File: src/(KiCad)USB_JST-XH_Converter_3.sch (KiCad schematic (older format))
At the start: 10 parts

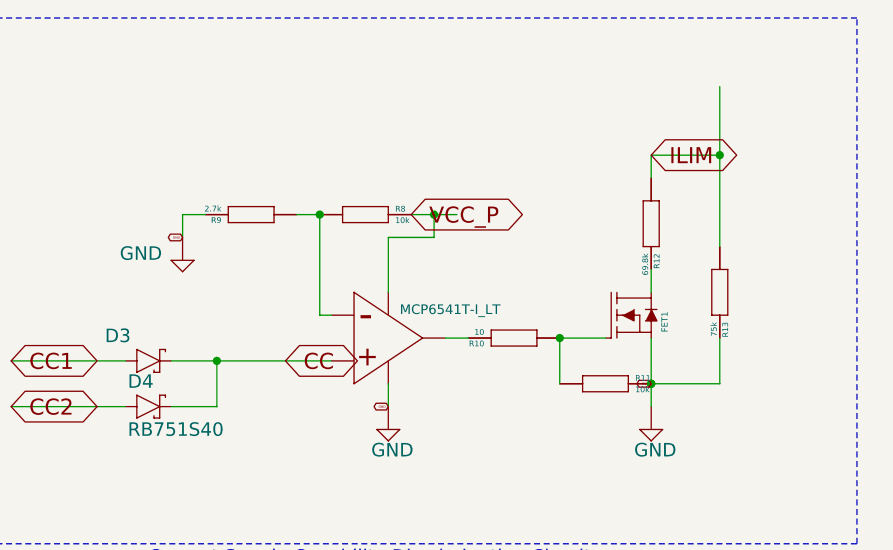
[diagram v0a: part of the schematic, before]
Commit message: 3Aモード用LEDの追加
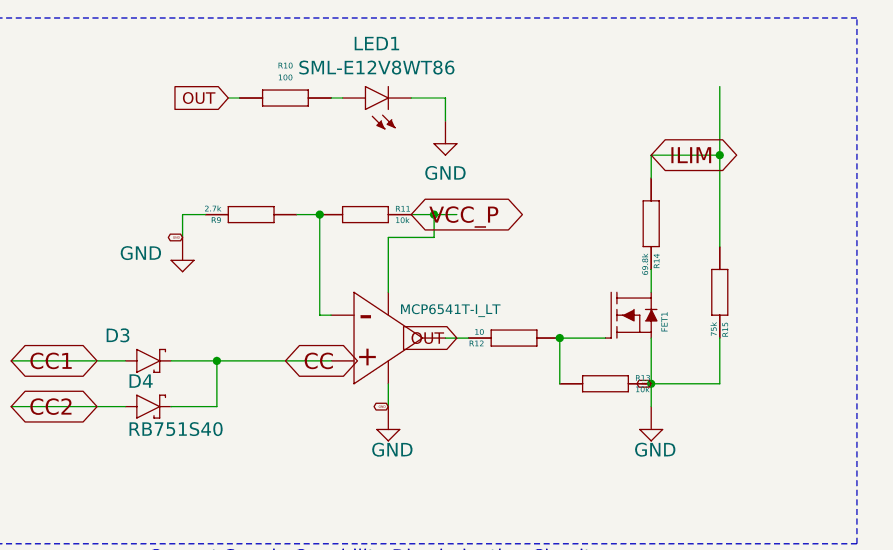
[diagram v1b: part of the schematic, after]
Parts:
- added LED1: SML-E12V8WT86, USB_JST-XH_Converter:SML-E12V8WT86, symbol USB_JST-XH_Converter-eagle-import:SML-E12V8WT86
- added R10: 100, USB_JST-XH_Converter:RG2012, symbol USB_JST-XH_Converter-eagle-import:RG2012
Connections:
- net labels added: OUT
- wire segments 29 -> 33
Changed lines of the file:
@@
 $Descr A4 11693 8268
 encoding utf-8
-Sheet 1 4
+Sheet 4 4
 Title ""
 Date ""
@@
 	7100 3700 6800 3700
 Connection ~ 6800 3700
-Connection ~ 6800 3700
 Text GLabel 6800 3700 0    10   BiDi ~ 0
 GND
@@
 AR Path="/5B1AAE1E" Ref="#FRAME3"  Part="1"
 AR Path="/639B4E7B/5B1AAE1E" Ref="#FRAME3"  Part="1"
+AR Path="/639ECBA2/5B1AAE1E" Ref="#FRAME3"  Part="1"
 F 0 "#FRAME3" H 2300 6000 50  0001 C CNN
 F 1 "A5L-LOC" H 2300 6000 50  0001 C CNN
@@
 AR Path="/3097C624" Ref="R8"  Part="1"
 AR Path="/639B4E7B/3097C624" Ref="R8"  Part="1"
-F 0 "R8" H 5680 2970 25  0000 L BNN
+AR Path="/639ECBA2/3097C624" Ref="R11"  Part="1"
+F 0 "R11" H 5680 2970 25  0000 L BNN
 F 1 "10k" H 5680 2920 25  0000 L BNN
 F 2 "USB_JST-XH_Converter:RG2012" H 5550 2960 50  0001 C CNN
@@
 AR Path="/1BCD2ED9" Ref="R9"  Part="1"
 AR Path="/639B4E7B/1BCD2ED9" Ref="R9"  Part="1"
+AR Path="/639ECBA2/1BCD2ED9" Ref="R9"  Part="1"
 F 0 "R9" H 5180 2970 25  0000 L BNN
 F 1 "2.7k" H 5180 2920 25  0000 L BNN
@@
 AR Path="/28999800" Ref="#SUPPLY10"  Part="1"
 AR Path="/639B4E7B/28999800" Ref="#SUPPLY010"  Part="1"
-F 0 "#SUPPLY010" H 4750 3160 50  0001 C CNN
+AR Path="/639ECBA2/28999800" Ref="#SUPPLY0111"  Part="1"
+F 0 "#SUPPLY0111" H 4750 3160 50  0001 C CNN
 F 1 "GND" H 4475 3155 59  0000 L BNN
 F 2 "" H 4750 3160 50  0001 C CNN
@@
 AR Path="/E0B04C0E" Ref="#SUPPLY11"  Part="1"
 AR Path="/639B4E7B/E0B04C0E" Ref="#SUPPLY011"  Part="1"
-F 0 "#SUPPLY011" H 5650 3900 50  0001 C CNN
+AR Path="/639ECBA2/E0B04C0E" Ref="#SUPPLY0112"  Part="1"
+F 0 "#SUPPLY0112" H 5650 3900 50  0001 C CNN
 F 1 "GND" H 5575 3775 59  0000 L BNN
 F 2 "" H 5650 3900 50  0001 C CNN
@@
 AR Path="/B5DC468C" Ref="R10"  Part="1"
 AR Path="/639B4E7B/B5DC468C" Ref="R10"  Part="1"
-F 0 "R10" H 6330 3510 25  0000 L BNN
+AR Path="/639ECBA2/B5DC468C" Ref="R12"  Part="1"
+F 0 "R12" H 6330 3510 25  0000 L BNN
 F 1 "10" H 6330 3460 25  0000 L BNN
 F 2 "USB_JST-XH_Converter:RG2012" H 6200 3500 50  0001 C CNN
@@
 AR Path="/369C72E5" Ref="R11"  Part="1"
 AR Path="/639B4E7B/369C72E5" Ref="R11"  Part="1"
-F 0 "R11" H 6730 3710 25  0000 L BNN
+AR Path="/639ECBA2/369C72E5" Ref="R13"  Part="1"
+F 0 "R13" H 6730 3710 25  0000 L BNN
 F 1 "10k" H 6730 3660 25  0000 L BNN
 F 2 "USB_JST-XH_Converter:RG2012" H 6600 3700 50  0001 C CNN
@@
 AR Path="/87B19EEA" Ref="R12"  Part="1"
 AR Path="/639B4E7B/87B19EEA" Ref="R12"  Part="1"
-F 0 "R12" H 6930 3010 25  0000 L BNN
+AR Path="/639ECBA2/87B19EEA" Ref="R14"  Part="1"
+F 0 "R14" H 6930 3010 25  0000 L BNN
 F 1 "69.8k" H 6930 2960 25  0000 L BNN
 F 2 "USB_JST-XH_Converter:RG2012" H 6800 3000 50  0001 C CNN
@@
 AR Path="/EFAC6E10" Ref="R13"  Part="1"
 AR Path="/639B4E7B/EFAC6E10" Ref="R13"  Part="1"
-F 0 "R13" H 7230 3310 25  0000 L BNN
+AR Path="/639ECBA2/EFAC6E10" Ref="R15"  Part="1"
+F 0 "R15" H 7230 3310 25  0000 L BNN
 F 1 "75k" H 7230 3260 25  0000 L BNN
 F 2 "USB_JST-XH_Converter:RG2012" H 7100 3300 50  0001 C CNN
@@
 AR Path="/31C2C8A5" Ref="#SUPPLY12"  Part="1"
 AR Path="/639B4E7B/31C2C8A5" Ref="#SUPPLY012"  Part="1"
-F 0 "#SUPPLY012" H 6800 3900 50  0001 C CNN
+AR Path="/639ECBA2/31C2C8A5" Ref="#SUPPLY0113"  Part="1"
+F 0 "#SUPPLY0113" H 6800 3900 50  0001 C CNN
 F 1 "GND" H 6725 3775 59  0000 L BNN
 F 2 "" H 6800 3900 50  0001 C CNN
@@
 AR Path="/93886C31" Ref="D3"  Part="1"
 AR Path="/639B4E7B/93886C31" Ref="D3"  Part="1"
+AR Path="/639ECBA2/93886C31" Ref="D3"  Part="1"
 F 0 "D3" H 4410 3675 59  0000 L BNN
 F 1 "RB751S40" H 4510 3465 59  0001 L BNN
@@
 AR Path="/04403A79" Ref="D4"  Part="1"
 AR Path="/639B4E7B/04403A79" Ref="D4"  Part="1"
+AR Path="/639ECBA2/04403A79" Ref="D4"  Part="1"
 F 0 "D4" H 4510 3875 59  0000 L BNN
 F 1 "RB751S40" H 4510 3665 59  0000 L BNN
@@
 AR Path="/931AB80C" Ref="COMP1"  Part="1"
 AR Path="/639B4E7B/931AB80C" Ref="COMP1"  Part="1"
+AR Path="/639ECBA2/931AB80C" Ref="COMP1"  Part="1"
 F 0 "COMP1" H 5500 3500 50  0001 C CNN
 F 1 "MCP6541T-I_LT" H 5700 3600 42  0000 L BNN
@@
 AR Path="/C50900C8" Ref="FET1"  Part="1"
 AR Path="/639B4E7B/C50900C8" Ref="FET1"  Part="1"
+AR Path="/639ECBA2/C50900C8" Ref="FET1"  Part="1"
 F 0 "FET1" V 6875 3325 27  0000 L BNN
 F 1 "BSS138" H 6800 3400 50  0001 C CNN
@@
 Text Notes 9100 5800 0    85   ~ 0
 完
+$Comp
+L USB_JST-XH_Converter-eagle-import:SML-E12V8WT86 LED1
+U 1 1 639EB85B
+P 5550 2450
+F 0 "LED1" V 5786 2400 59  0000 C CNN
+F 1 "SML-E12V8WT86" V 5681 2400 59  0000 C CNN
+F 2 "USB_JST-XH_Converter:SML-E12V8WT86" H 5550 2450 50  0001 C CNN
+F 3 "" H 5550 2450 50  0001 C CNN
+	1    5550 2450
+	0    -1   -1   0
+$EndComp
+Text GLabel 5950 3500 0    50   Input ~ 0
+OUT
+Text GLabel 4950 2450 0    50   Input ~ 0
+OUT
+$Comp
+L USB_JST-XH_Converter-eagle-import:RG2012 R10
+U 1 1 639F548F
+P 5200 2450
+F 0 "R10" H 5200 2591 25  0000 C CNN
+F 1 "100" H 5200 2539 25  0000 C CNN
+F 2 "USB_JST-XH_Converter:RG2012" H 5200 2450 50  0001 C CNN
+F 3 "" H 5200 2450 50  0001 C CNN
+	1    5200 2450
+	1    0    0    -1
+$EndComp
+Wire Wire Line
+	5000 2450 4950 2450
+Wire Wire Line
+	5400 2450 5450 2450
+$Comp
+L USB_JST-XH_Converter-eagle-import:GND #SUPPLY0114
+U 1 1 639F6F3D
+P 5900 2650
+F 0 "#SUPPLY0114" H 5900 2650 50  0001 C CNN
+F 1 "GND" H 5900 2520 59  0000 C CNN
+F 2 "" H 5900 2650 50  0001 C CNN
+F 3 "" H 5900 2650 50  0001 C CNN
+	1    5900 2650
+	1    0    0    -1
+$EndComp
+Wire Wire Line
+	5750 2450 5900 2450
+Wire Wire Line
+	5900 2450 5900 2550
 $EndSCHEMATC
